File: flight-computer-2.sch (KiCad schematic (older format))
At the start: 73 parts

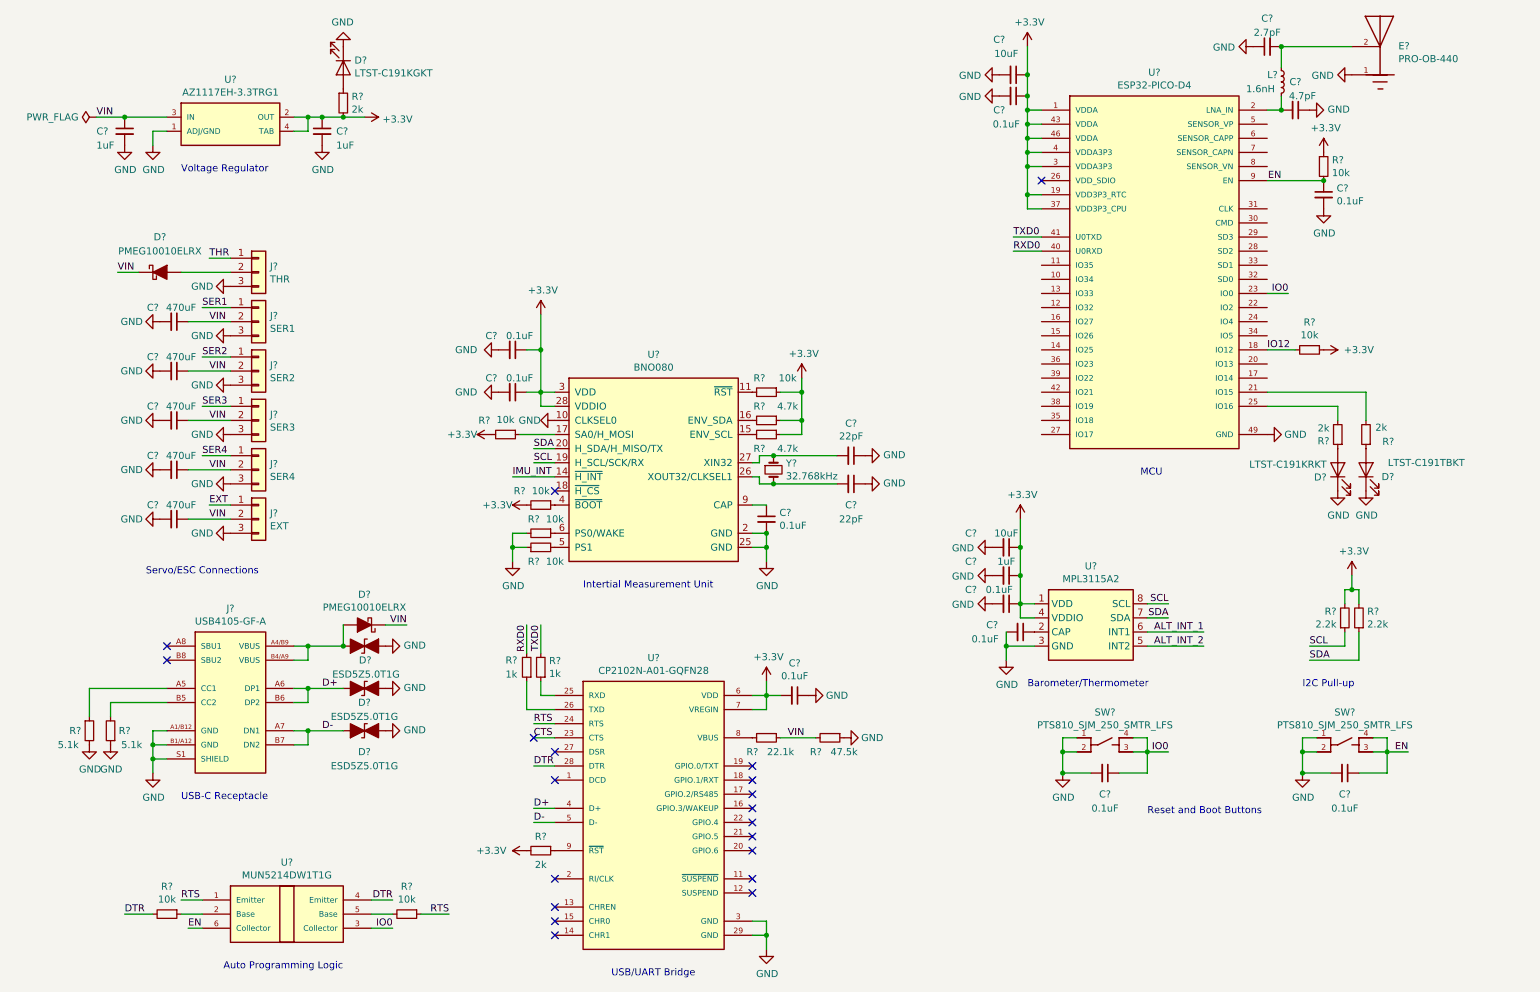
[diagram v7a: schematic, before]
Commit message: Switched diode and added current limiting resistors
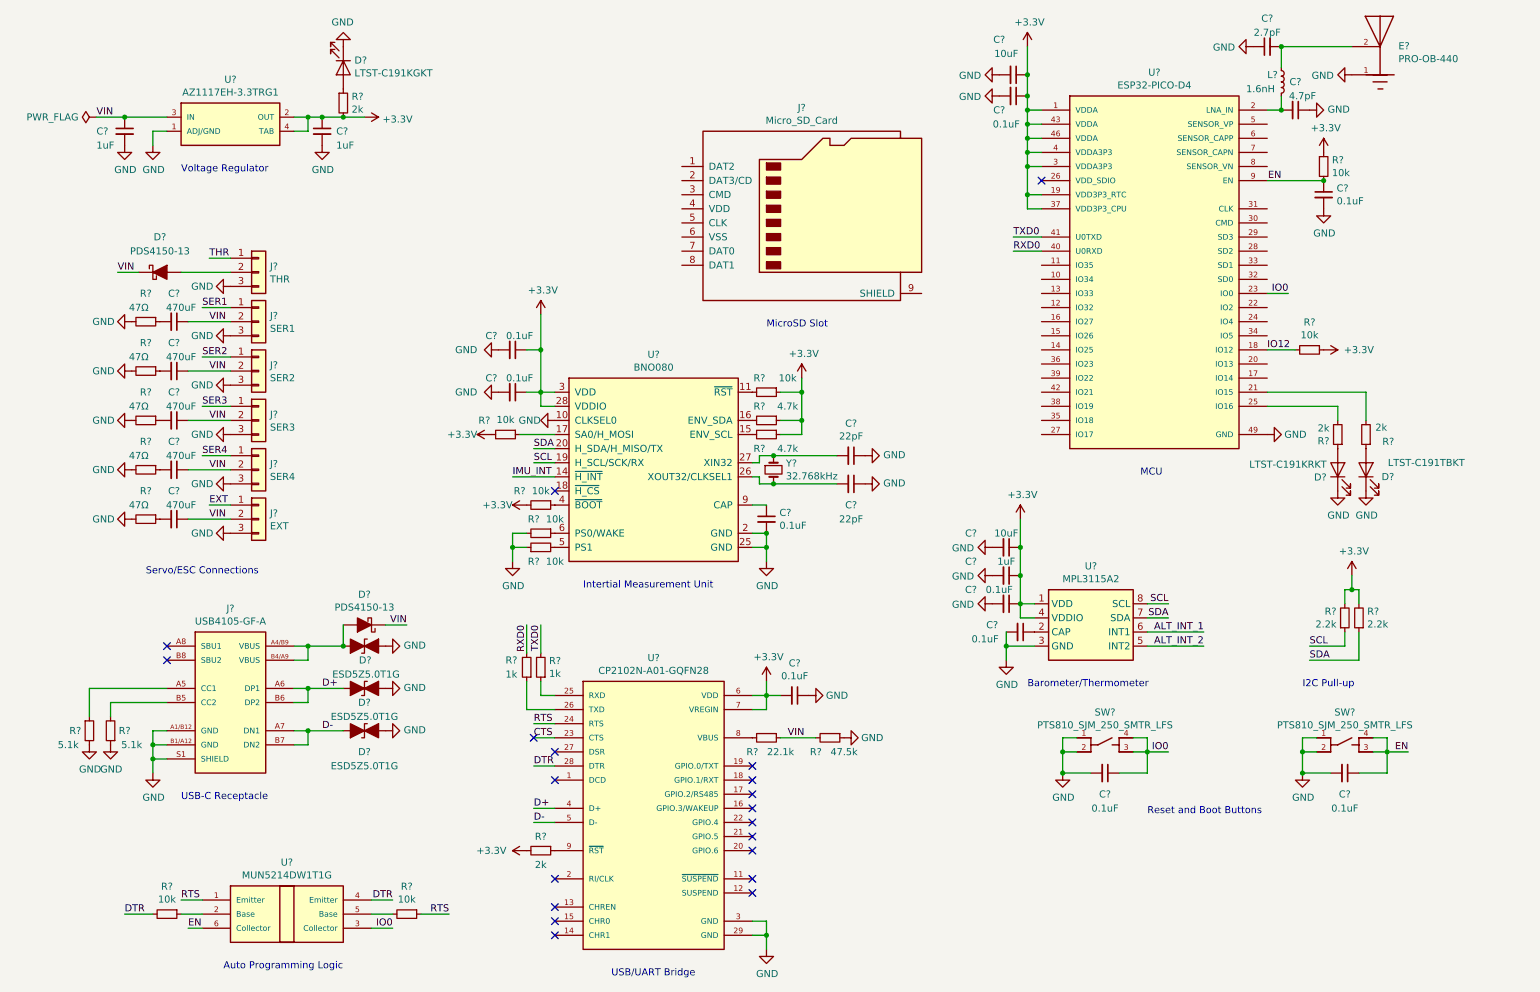
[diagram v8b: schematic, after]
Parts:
- removed C? (x4): 470uF, symbol Device:C_Small
- added C? (x4): 470uF, symbol Device:C_Small
- added J?: Micro_SD_Card, symbol Connector:Micro_SD_Card
- added R? (x5): 47Ω, symbol Device:R_Small
- D? (x2): value PMEG10010ELRX -> PDS4150-13
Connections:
- net GND: now also R?.2, R?.2, R?.2, R?.2, R?.2; no longer C?.2
- net VIN: now also C?.1, C?.1, C?.1, C?.1
- new net: C?.2, R?.1 (x5)
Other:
- note added: "MicroSD Slot"
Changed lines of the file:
@@
 P 3000 5000
 F 0 "D?" H 3000 4784 50  0000 C CNN
-F 1 "PMEG10010ELRX" H 3000 4875 50  0000 C CNN
+F 1 "PDS4150-13" H 3000 4875 50  0000 C CNN
 F 2 "" H 3000 5000 50  0001 C CNN
 F 3 "~" H 3000 5000 50  0001 C CNN
@@
 P 1550 2500
 F 0 "D?" H 1550 2750 50  0000 C CNN
-F 1 "PMEG10010ELRX" H 1550 2650 50  0000 C CNN
+F 1 "PDS4150-13" H 1550 2650 50  0000 C CNN
 F 2 "" H 1550 2500 50  0001 C CNN
 F 3 "~" H 1550 2500 50  0001 C CNN
@@
 U 1 1 5F833B8D
 P 1650 2850
-F 0 "C?" V 1550 2700 50  0000 C CNN
+F 0 "C?" V 1450 2850 50  0000 C CNN
 F 1 "470uF" V 1550 2900 50  0000 C CNN
 F 2 "" H 1650 2850 50  0001 C CNN
@@
 L power:GND #PWR?
 U 1 1 5F8345F6
-P 1550 2850
-F 0 "#PWR?" H 1550 2600 50  0001 C CNN
-F 1 "GND" V 1550 2650 50  0000 C CNN
-F 2 "" H 1550 2850 50  0001 C CNN
-F 3 "" H 1550 2850 50  0001 C CNN
-	1    1550 2850
+P 1350 2850
+F 0 "#PWR?" H 1350 2600 50  0001 C CNN
+F 1 "GND" V 1350 2650 50  0000 C CNN
+F 2 "" H 1350 2850 50  0001 C CNN
+F 3 "" H 1350 2850 50  0001 C CNN
+	1    1350 2850
 	0    1    1    0
 $EndComp
@@
 Wire Wire Line
 	1850 2750 2050 2750
-$Comp
-L Device:C_Small C?
-U 1 1 5F84AD56
-P 1650 3200
-F 0 "C?" V 1550 3050 50  0000 C CNN
-F 1 "470uF" V 1550 3250 50  0000 C CNN
-F 2 "" H 1650 3200 50  0001 C CNN
-F 3 "~" H 1650 3200 50  0001 C CNN
-	1    1650 3200
-	0    1    1    0
-$EndComp
-$Comp
-L Device:C_Small C?
-U 1 1 5F84B24D
-P 1650 3550
-F 0 "C?" V 1550 3400 50  0000 C CNN
-F 1 "470uF" V 1550 3600 50  0000 C CNN
-F 2 "" H 1650 3550 50  0001 C CNN
-F 3 "~" H 1650 3550 50  0001 C CNN
-	1    1650 3550
-	0    1    1    0
-$EndComp
-$Comp
-L Device:C_Small C?
-U 1 1 5F84B6D1
-P 1650 3900
-F 0 "C?" V 1550 3750 50  0000 C CNN
-F 1 "470uF" V 1550 3950 50  0000 C CNN
-F 2 "" H 1650 3900 50  0001 C CNN
-F 3 "~" H 1650 3900 50  0001 C CNN
-	1    1650 3900
-	0    1    1    0
-$EndComp
-$Comp
-L Device:C_Small C?
-U 1 1 5F84BB10
-P 1650 4250
-F 0 "C?" V 1550 4100 50  0000 C CNN
-F 1 "470uF" V 1550 4300 50  0000 C CNN
-F 2 "" H 1650 4250 50  0001 C CNN
-F 3 "~" H 1650 4250 50  0001 C CNN
-	1    1650 4250
-	0    1    1    0
-$EndComp
-$Comp
-L power:GND #PWR?
-U 1 1 5F84BEAE
-P 1550 3200
-F 0 "#PWR?" H 1550 2950 50  0001 C CNN
-F 1 "GND" V 1550 3000 50  0000 C CNN
-F 2 "" H 1550 3200 50  0001 C CNN
-F 3 "" H 1550 3200 50  0001 C CNN
-	1    1550 3200
-	0    1    1    0
-$EndComp
-$Comp
-L power:GND #PWR?
-U 1 1 5F84C0E2
-P 1550 3550
-F 0 "#PWR?" H 1550 3300 50  0001 C CNN
-F 1 "GND" V 1550 3350 50  0000 C CNN
-F 2 "" H 1550 3550 50  0001 C CNN
-F 3 "" H 1550 3550 50  0001 C CNN
-	1    1550 3550
-	0    1    1    0
-$EndComp
-$Comp
-L power:GND #PWR?
-U 1 1 5F84C37C
-P 1550 3900
-F 0 "#PWR?" H 1550 3650 50  0001 C CNN
-F 1 "GND" V 1550 3700 50  0000 C CNN
-F 2 "" H 1550 3900 50  0001 C CNN
-F 3 "" H 1550 3900 50  0001 C CNN
-	1    1550 3900
-	0    1    1    0
-$EndComp
-$Comp
-L power:GND #PWR?
-U 1 1 5F84C65A
-P 1550 4250
-F 0 "#PWR?" H 1550 4000 50  0001 C CNN
-F 1 "GND" V 1550 4050 50  0000 C CNN
-F 2 "" H 1550 4250 50  0001 C CNN
-F 3 "" H 1550 4250 50  0001 C CNN
-	1    1550 4250
-	0    1    1    0
-$EndComp
 Wire Wire Line
 	1750 3200 2050 3200
@@
 Text Notes 9650 5450 0    50   ~ 0
 I2C Pull-up
+$Comp
+L Connector:Micro_SD_Card J?
+U 1 1 5FAF6E41
+P 6150 2050
+F 0 "J?" H 6100 2767 50  0000 C CNN
+F 1 "Micro_SD_Card" H 6100 2676 50  0000 C CNN
+F 2 "" H 7300 2350 50  0001 C CNN
+F 3 "http://katalog.we-online.de/em/datasheet/693072010801.pdf" H 6150 2050 50  0001 C CNN
+	1    6150 2050
+	1    0    0    -1
+$EndComp
+Text Notes 5850 2900 0    50   ~ 0
+MicroSD Slot
+$Comp
+L Device:R_Small R?
+U 1 1 5FAFB86F
+P 1450 2850
+F 0 "R?" V 1250 2850 50  0000 C CNN
+F 1 "47Ω" V 1350 2800 50  0000 C CNN
+F 2 "" H 1450 2850 50  0001 C CNN
+F 3 "~" H 1450 2850 50  0001 C CNN
+	1    1450 2850
+	0    1    1    0
+$EndComp
+$Comp
+L Device:C_Small C?
+U 1 1 5FAFD4E9
+P 1650 3200
+F 0 "C?" V 1450 3200 50  0000 C CNN
+F 1 "470uF" V 1550 3250 50  0000 C CNN
+F 2 "" H 1650 3200 50  0001 C CNN
+F 3 "~" H 1650 3200 50  0001 C CNN
+	1    1650 3200
+	0    1    1    0
+$EndComp
+$Comp
+L Device:C_Small C?
+U 1 1 5FAFD93F
+P 1650 3550
+F 0 "C?" V 1450 3550 50  0000 C CNN
+F 1 "470uF" V 1550 3600 50  0000 C CNN
+F 2 "" H 1650 3550 50  0001 C CNN
+F 3 "~" H 1650 3550 50  0001 C CNN
+	1    1650 3550
+	0    1    1    0
+$EndComp
+$Comp
+L Device:C_Small C?
+U 1 1 5FAFDE7B
+P 1650 3900
+F 0 "C?" V 1450 3900 50  0000 C CNN
+F 1 "470uF" V 1550 3950 50  0000 C CNN
+F 2 "" H 1650 3900 50  0001 C CNN
+F 3 "~" H 1650 3900 50  0001 C CNN
+	1    1650 3900
+	0    1    1    0
+$EndComp
+$Comp
+L Device:C_Small C?
+U 1 1 5FAFE219
+P 1650 4250
+F 0 "C?" V 1450 4250 50  0000 C CNN
+F 1 "470uF" V 1550 4300 50  0000 C CNN
+F 2 "" H 1650 4250 50  0001 C CNN
+F 3 "~" H 1650 4250 50  0001 C CNN
+	1    1650 4250
+	0    1    1    0
+$EndComp
+$Comp
+L Device:R_Small R?
+U 1 1 5FAFE62A
+P 1450 3200
+F 0 "R?" V 1250 3200 50  0000 C CNN
+F 1 "47Ω" V 1350 3150 50  0000 C CNN
+F 2 "" H 1450 3200 50  0001 C CNN
+F 3 "~" H 1450 3200 50  0001 C CNN
+	1    1450 3200
+	0    1    1    0
+$EndComp
+$Comp
+L Device:R_Small R?
+U 1 1 5FAFEA43
+P 1450 3550
+F 0 "R?" V 1250 3550 50  0000 C CNN
+F 1 "47Ω" V 1350 3500 50  0000 C CNN
+F 2 "" H 1450 3550 50  0001 C CNN
+F 3 "~" H 1450 3550 50  0001 C CNN
+	1    1450 3550
+	0    1    1    0
+$EndComp
+$Comp
+L Device:R_Small R?
+U 1 1 5FAFEEEF
+P 1450 3900
+F 0 "R?" V 1250 3900 50  0000 C CNN
+F 1 "47Ω" V 1350 3850 50  0000 C CNN
+F 2 "" H 1450 3900 50  0001 C CNN
+F 3 "~" H 1450 3900 50  0001 C CNN
+	1    1450 3900
+	0    1    1    0
+$EndComp
+$Comp
+L Device:R_Small R?
+U 1 1 5FAFF347
+P 1450 4250
+F 0 "R?" V 1250 4250 50  0000 C CNN
+F 1 "47Ω" V 1350 4200 50  0000 C CNN
+F 2 "" H 1450 4250 50  0001 C CNN
+F 3 "~" H 1450 4250 50  0001 C CNN
+	1    1450 4250
+	0    1    1    0
+$EndComp
+$Comp
+L power:GND #PWR?
+U 1 1 5FAFF74B
+P 1350 3200
+F 0 "#PWR?" H 1350 2950 50  0001 C CNN
+F 1 "GND" V 1350 3000 50  0000 C CNN
+F 2 "" H 1350 3200 50  0001 C CNN
+F 3 "" H 1350 3200 50  0001 C CNN
+	1    1350 3200
+	0    1    1    0
+$EndComp
+$Comp
+L power:GND #PWR?
+U 1 1 5FAFFA38
+P 1350 3550
+F 0 "#PWR?" H 1350 3300 50  0001 C CNN
+F 1 "GND" V 1350 3350 50  0000 C CNN
+F 2 "" H 1350 3550 50  0001 C CNN
+F 3 "" H 1350 3550 50  0001 C CNN
+	1    1350 3550
+	0    1    1    0
+$EndComp
+$Comp
+L power:GND #PWR?
+U 1 1 5FAFFD8B
+P 1350 3900
+F 0 "#PWR?" H 1350 3650 50  0001 C CNN
+F 1 "GND" V 1350 3700 50  0000 C CNN
+F 2 "" H 1350 3900 50  0001 C CNN
+F 3 "" H 1350 3900 50  0001 C CNN
+	1    1350 3900
+	0    1    1    0
+$EndComp
+$Comp
+L power:GND #PWR?
+U 1 1 5FB000DE
+P 1350 4250
+F 0 "#PWR?" H 1350 4000 50  0001 C CNN
+F 1 "GND" V 1350 4050 50  0000 C CNN
+F 2 "" H 1350 4250 50  0001 C CNN
+F 3 "" H 1350 4250 50  0001 C CNN
+	1    1350 4250
+	0    1    1    0
+$EndComp
 $EndSCHEMATC
